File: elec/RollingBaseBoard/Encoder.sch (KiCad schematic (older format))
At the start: 6 parts, among them P7 Encoder

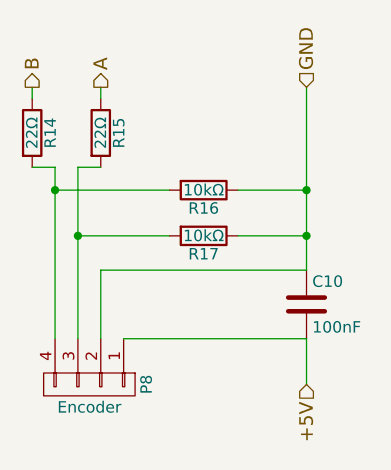
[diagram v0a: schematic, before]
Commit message: Updated the schematics to use the proper footprints.
Also regenerated the net list file.
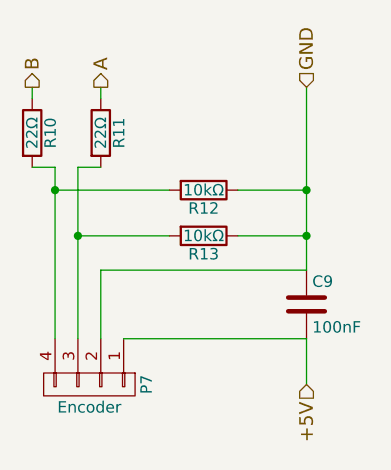
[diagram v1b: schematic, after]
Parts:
- C9: footprint (none) -> Footprints:C_CMS0603
- P7: footprint (none) -> Footprints:Conn_01x04
- R10, R11, R12, R13: footprint (none) -> Footprints:R_CMS1206
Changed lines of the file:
@@
 $Descr A4 11693 8268
 encoding utf-8
-Sheet 8 17
+Sheet 7 17
 Title ""
 Date ""
@@
 AR Path="/55E78073/55E71CE3" Ref="P7"  Part="1"
 AR Path="/55E78AE8/55E71CE3" Ref="P8"  Part="1"
-F 0 "P8" H 5850 4550 50  0000 C CNN
+F 0 "P7" H 5850 4550 50  0000 C CNN
 F 1 "Encoder" V 5950 4300 50  0000 C CNN
-F 2 "" H 5850 4300 60  0000 C CNN
+F 2 "Footprints:Conn_01x04" H 5850 4300 60  0001 C CNN
 F 3 "" H 5850 4300 60  0000 C CNN
 	1    5850 4300
@@
 AR Path="/55E78073/55E71CEC" Ref="C9"  Part="1"
 AR Path="/55E78AE8/55E71CEC" Ref="C10"  Part="1"
-F 0 "C10" H 6825 4050 50  0000 L CNN
+F 0 "C9" H 6825 4050 50  0000 L CNN
 F 1 "100nF" H 6825 3850 50  0000 L CNN
-F 2 "" H 6838 3800 30  0000 C CNN
+F 2 "Footprints:C_CMS0603" H 6838 3800 30  0001 C CNN
 F 3 "" H 6800 3950 60  0000 C CNN
 	1    6800 3950
@@
 AR Path="/55E78073/5602AF11" Ref="R10"  Part="1"
 AR Path="/55E78AE8/5602AF11" Ref="R14"  Part="1"
-F 0 "R14" V 5680 3200 50  0000 C CNN
+F 0 "R10" V 5680 3200 50  0000 C CNN
 F 1 "22Ω" V 5600 3200 50  0000 C CNN
-F 2 "" V 5530 3200 30  0000 C CNN
+F 2 "Footprints:R_CMS1206" V 5530 3200 30  0001 C CNN
 F 3 "" H 5600 3200 30  0000 C CNN
 	1    5600 3200
@@
 AR Path="/55E78073/5602AF44" Ref="R11"  Part="1"
 AR Path="/55E78AE8/5602AF44" Ref="R15"  Part="1"
-F 0 "R15" V 5980 3200 50  0000 C CNN
+F 0 "R11" V 5980 3200 50  0000 C CNN
 F 1 "22Ω" V 5900 3200 50  0000 C CNN
-F 2 "" V 5830 3200 30  0000 C CNN
+F 2 "Footprints:R_CMS1206" V 5830 3200 30  0001 C CNN
 F 3 "" H 5900 3200 30  0000 C CNN
 	1    5900 3200
@@
 AR Path="/55E78073/5602B19C" Ref="R13"  Part="1"
 AR Path="/55E78AE8/5602B19C" Ref="R17"  Part="1"
-F 0 "R17" V 6430 3650 50  0000 C CNN
+F 0 "R13" V 6430 3650 50  0000 C CNN
 F 1 "10kΩ" V 6350 3650 50  0000 C CNN
-F 2 "" V 6280 3650 30  0000 C CNN
+F 2 "Footprints:R_CMS1206" V 6280 3650 30  0001 C CNN
 F 3 "" H 6350 3650 30  0000 C CNN
 	1    6350 3650
@@
 AR Path="/55E78073/5602B1C5" Ref="R12"  Part="1"
 AR Path="/55E78AE8/5602B1C5" Ref="R16"  Part="1"
-F 0 "R16" V 6430 3450 50  0000 C CNN
+F 0 "R12" V 6430 3450 50  0000 C CNN
 F 1 "10kΩ" V 6350 3450 50  0000 C CNN
-F 2 "" V 6280 3450 30  0000 C CNN
+F 2 "Footprints:R_CMS1206" V 6280 3450 30  0001 C CNN
 F 3 "" H 6350 3450 30  0000 C CNN
 	1    6350 3450
